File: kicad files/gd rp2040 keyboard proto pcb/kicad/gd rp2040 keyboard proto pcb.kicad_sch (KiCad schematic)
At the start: 49 parts, among them J1 USB Pwr, J10 CTRL1-HDR, J11 CTRL2-HDR, J12 USB_A, J14 GPIO, J2 Power Sequence, J3 Power, J4 FTDI Header, J5 CTRL1, J6 CTRL2, J7 Addr_Main_Data, J9 Addr_Main_Data-HDR, SW1 2040 RESET, SW2 MEGA POWER, U1 MIC5504-3.3YM5, U2 W25Q128JVS, U3 RP2040, U4 74HC245, U6 74LVC2G08DP-Q100H, U7 74LVC2G08DP-Q100H, U8 74LVC2G08DP-Q100H, Y1 ECS-120-18-33-JEM-TR

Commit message: almost done...
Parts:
- removed U6, U7, U8: 74LVC2G08DP-Q100H, Package_SO:TSSOP-8_3x3mm_P0.65mm, symbol 74xGxx:74LVC2G08
- added D5: 5V_PWR, LED_SMD:LED_1206_3216Metric, symbol My Library:D_1206
- added D8: 3V3_PWR, LED_SMD:LED_1206_3216Metric, symbol My Library:D_1206
- added Q9: BC817, Package_TO_SOT_SMD:SOT-23, symbol Transistor_BJT:BC817
- added R20, R23: 1K, Resistor_SMD:R_0805_2012Metric, symbol My_Library:R_0805
- added R28, R29: 4k7, Resistor_SMD:R_0805_2012Metric, symbol My_Library:R_0805
- added TP1, TP2, TP3: TestPoint_Harwin, My Libraries:Harwin-S1751-46-Test-Point, symbol My Library:TestPoint_Harwin
- added U10, U11, U14: 74LVC2G04, Package_TO_SOT_SMD:SOT-363_SC-70-6, symbol 74xGxx:74LVC2G04
- added U12, U13: 74LVC2G32, Package_SO:VSSOP-8_2.4x2.1mm_P0.5mm, symbol 74xGxx:74LVC2G32
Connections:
- net +3V3: now also R23.1, TP2.1, U10.5 (+3V3), U10.5 (+3V3), U11.5 (+3V3), U11.5 (+3V3), U12.8 (+3V3), U12.8 (+3V3), U13.8 (+3V3), U13.8 (+3V3), U14.5 (+3V3), U14.5 (+3V3)
- net +5V: now also R20.1, R29.2, TP1.1
- net 245_EN: now also TP3.1
- net GND: now also D5.1 (K), D8.1 (K), Q9.2 (E), U10.2 (GND), U10.2 (GND), U11.2 (GND), U11.2 (GND), U12.4 (GND), U12.4 (GND), U13.4 (GND), U13.4 (GND), U13.5, U13.6, U14.2 (GND), U14.2 (GND)
- net KSEL0: now also U13.2
- net KSEL0rp: now also U13.7
- net KSEL1: now also U12.6
- net KSEL1rp: now also U12.3
- net KSEL2: now also U12.2
- net KSEL2rp: now also U12.7
- net PH0: now also U14.1
- net PH0rp: now also U14.4
- net RESETrp: now also U11.6
- net RW: now also U10.3
- net RWrp: now also U10.6
- net ~{RESET}: now also Q9.3 (C), R29.1, U11.3
- net GPIO18: no longer names the net of J14.6 (Pin_6)
- net GPIO18: no longer U3.29 (GPIO18)
- net TXen: no longer names the net of U3.37 (GPIO25)
- new net: Q9.1 (B), R28.1
- new net: D5.2 (A), R20.2
- new net: D8.2 (A), R23.2
- new net: U11.1, U11.4
- new net: U10.1, U10.4
- new net RESET_CTL: R28.2, U3.29 (GPIO18)
- new net ~{PH0}: U12.1, U12.5, U13.1, U14.3, U14.6
- no-connect marks 0 -> 1
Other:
- moved on the sheet: C2, C3, Ctx1, Ctx2, J14, R5, Y1

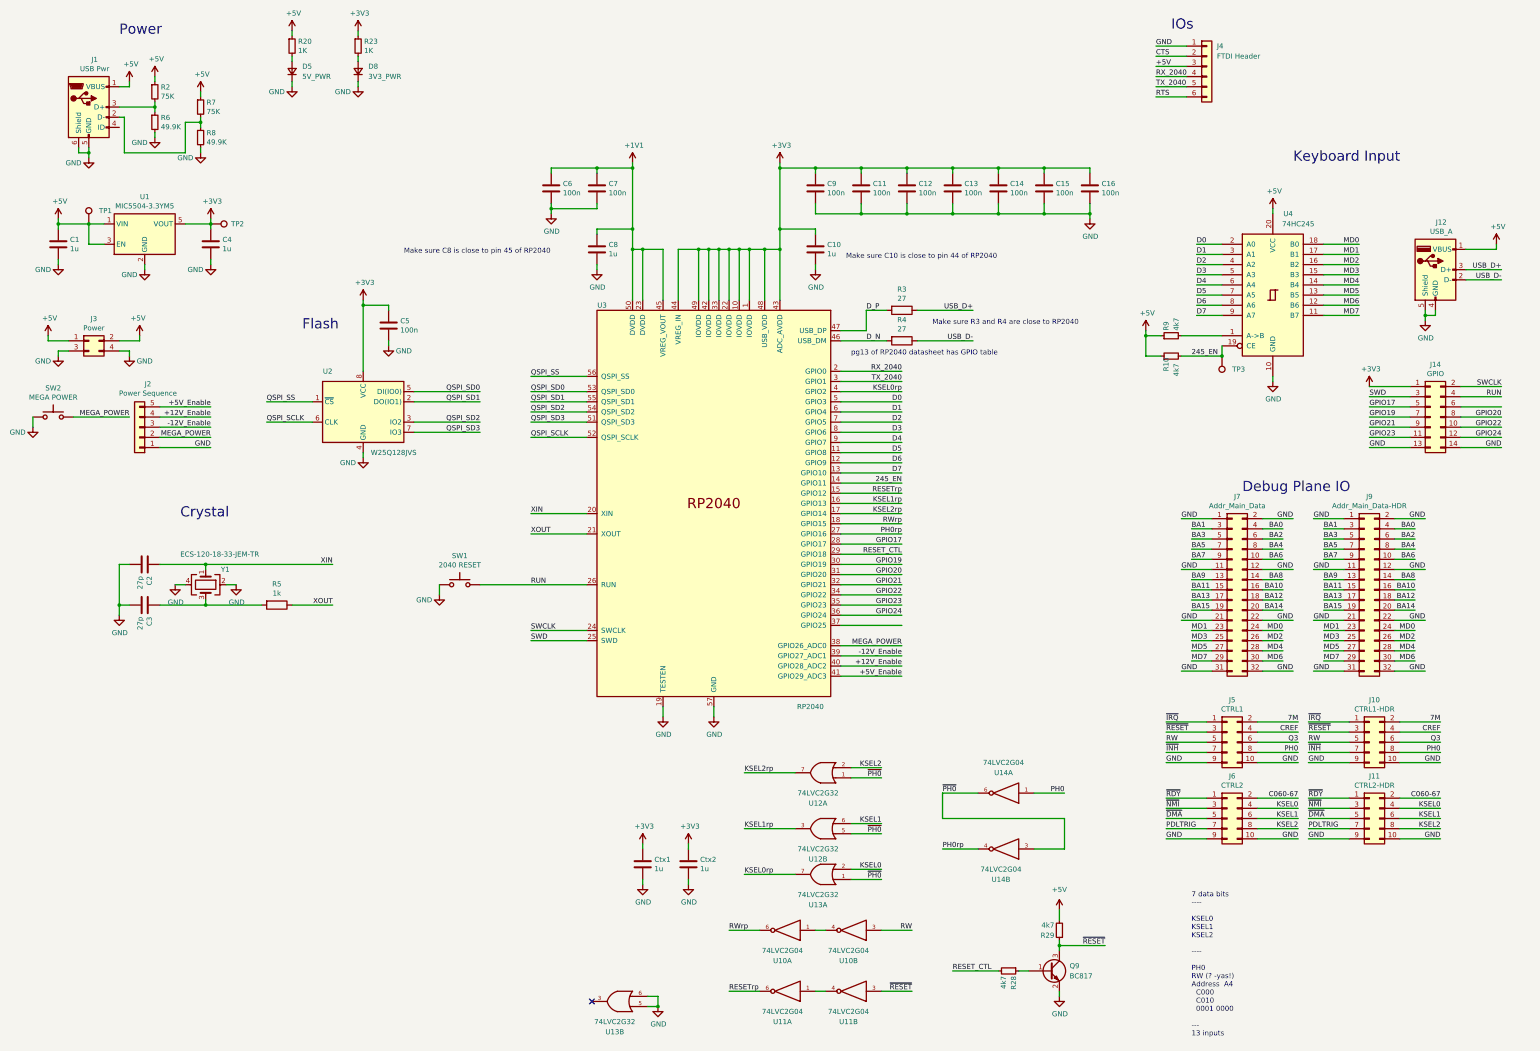
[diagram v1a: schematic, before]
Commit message: rev3 with 573 buffer for gating KSEL and RW
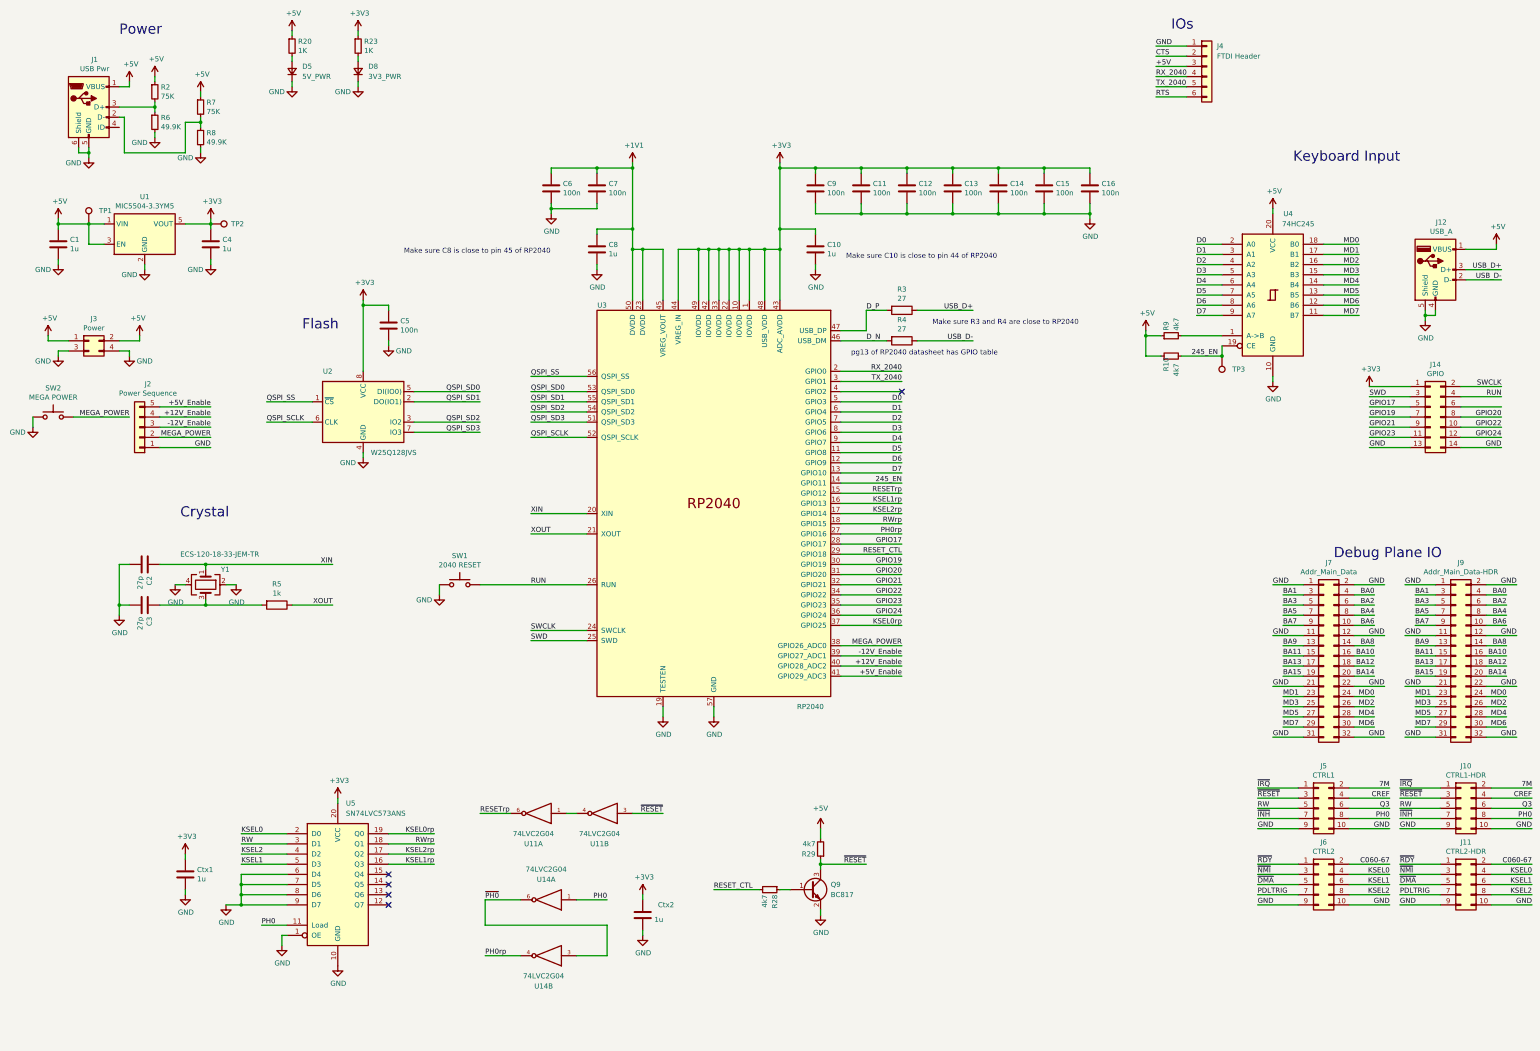
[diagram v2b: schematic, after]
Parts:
- removed U10: 74LVC2G04, Package_TO_SOT_SMD:SOT-363_SC-70-6, symbol 74xGxx:74LVC2G04
- removed U12, U13: 74LVC2G32, Package_SO:VSSOP-8_2.4x2.1mm_P0.5mm, symbol 74xGxx:74LVC2G32
- added U5: SN74LVC573ANS, Package_SO:SO-20_5.3x12.6mm_P1.27mm, symbol 74xx:74LS573
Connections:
- net +3V3: now also U5.20 (VCC)
- net GND: now also U5.1 (OE), U5.10 (GND), U5.6 (D4), U5.7 (D5), U5.8 (D6), U5.9 (D7)
- net KSEL0: now also U5.2 (D0)
- net KSEL0rp: now also U3.37 (GPIO25), U5.19 (Q0); no longer U3.4 (GPIO2)
- net KSEL1: now also U5.5 (D3)
- net KSEL1rp: now also U5.16 (Q3)
- net KSEL2: now also U5.4 (D2)
- net KSEL2rp: now also U5.17 (Q2)
- net PH0: now also U5.11 (Load)
- net RW: now also U5.3 (D1)
- net RWrp: now also U5.18 (Q1)
- no-connect marks 1 -> 5
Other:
- note removed: "7 data bits ---- KSEL0 KSEL1 KSEL2 ---- PH0 RW (? -yas!) Address A4 C000 C010 0001 0000 --- 13 inputs"
- company: (none) -> twitch.tv/baldengineer
- title: RP2040 for Mini IIe Proto -> RP2040 for Mega IIe Proto Rev2
- moved on the sheet: Ctx1, Ctx2, J10, J11, J5, J6, J7, J9, Q9, R28, R29, U11A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

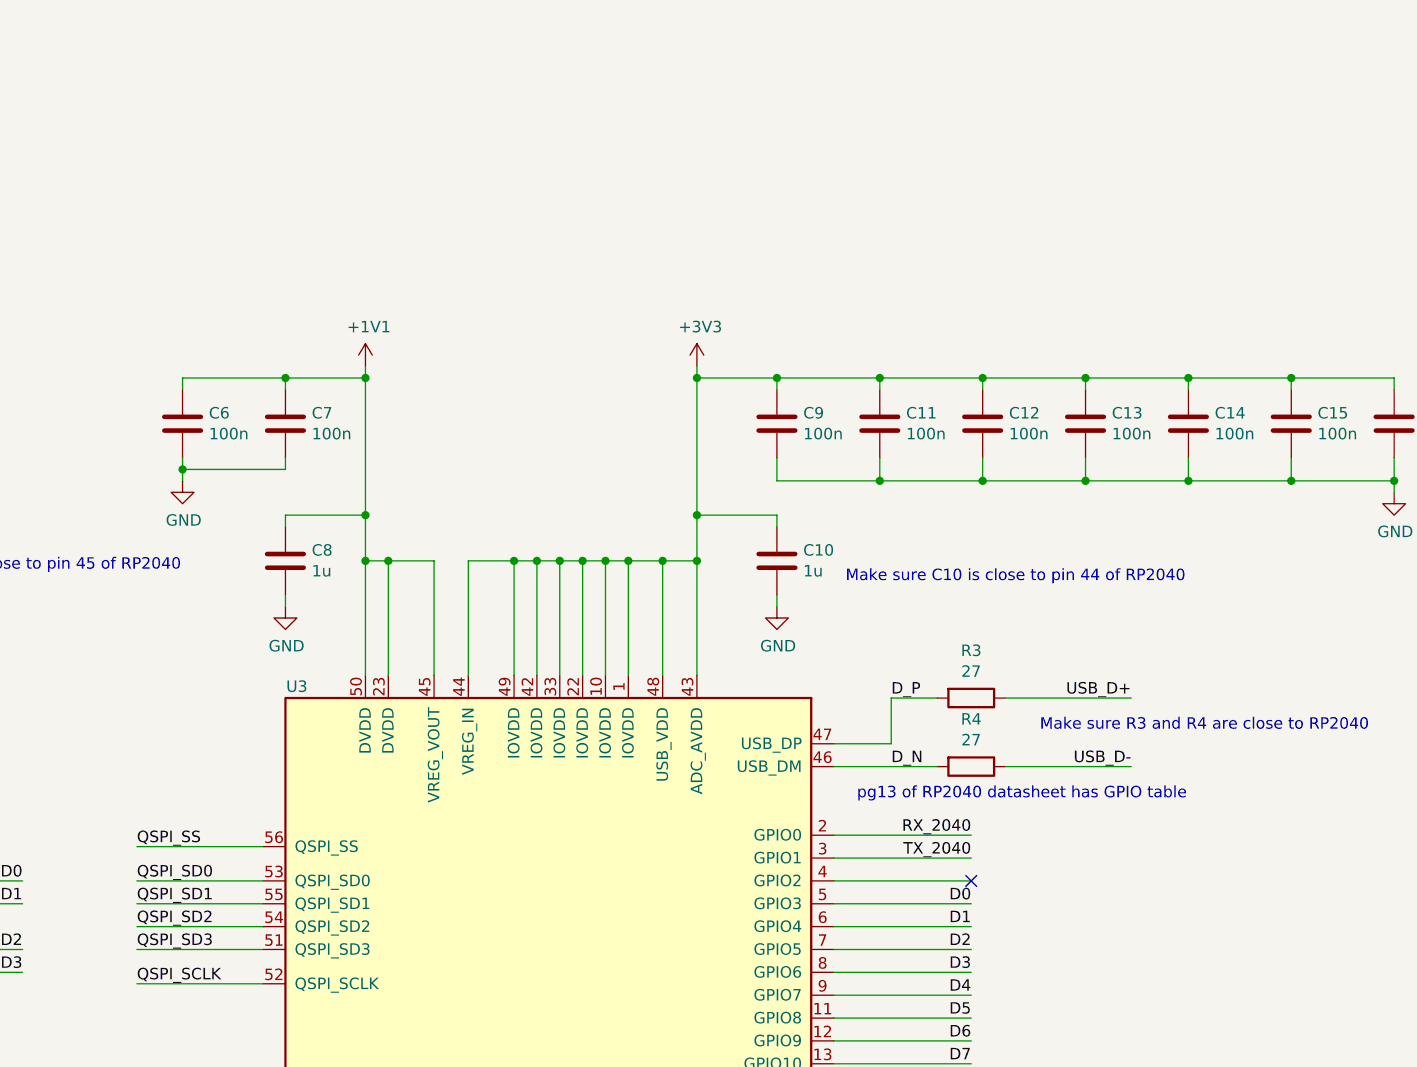
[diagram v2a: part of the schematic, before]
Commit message: added test point for GPIO2 (former KSEL0) -- Tim said I could!
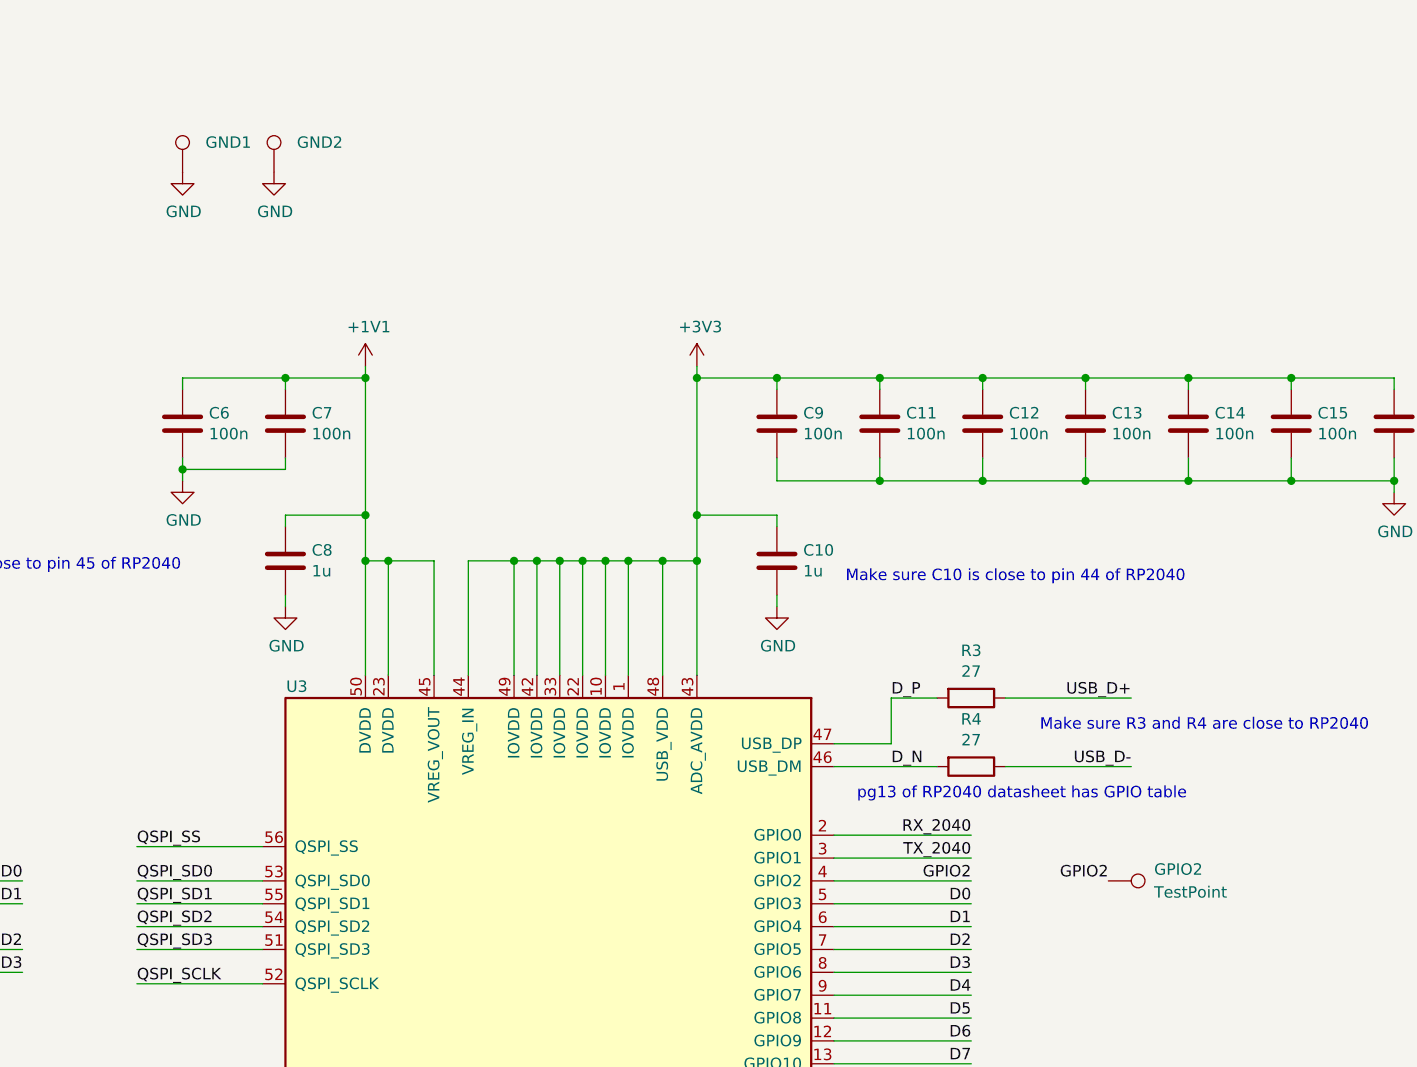
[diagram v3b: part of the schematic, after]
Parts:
- added GND1, GND2: TestPoint_Harwin, My Libraries:Harwin-S1751-46-Test-Point, symbol My Library:TestPoint_Harwin
- added GPIO2: TestPoint, TestPoint:TestPoint_Pad_D1.0mm, symbol Connector:TestPoint
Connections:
- net GND: now also GND1.1, GND2.1
- net GPIO2: now reaches U3.4 (GPIO2)
- net GPIO2: now also GPIO2.1
- no-connect marks 5 -> 4
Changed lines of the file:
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@@
   (junction (at 199.39 81.28) (diameter 0) (color 0 0 0 0)
   )
-  (no_connect (at 245.11 116.84))
   (no_connect (at 116.84 240.03))
   (no_connect (at 116.84 237.49))
@@
     (stroke (width 0) (type default) (color 0 0 0 0))
   )
-  (wire (pts (xy 229.87 116.84) (xy 245.11 116.84))
-    (stroke (width 0) (type default) (color 0 0 0 0))
-  )
   (wire (pts (xy 80.01 229.87) (xy 91.44 229.87))
     (stroke (width 0) (type default) (color 0 0 0 0))
@@
     (stroke (width 0) (type default) (color 0 0 0 0))
   )
+  (wire (pts (xy 229.87 116.84) (xy 245.11 116.84))
+    (stroke (width 0) (type default) (color 0 0 0 0))
+  )
   (wire (pts (xy 391.16 198.12) (xy 396.24 198.12))
     (stroke (width 0) (type default) (color 0 0 0 0))
@@
     (effects (font (size 1.27 1.27)) (justify left bottom))
   )
+  (label "GPIO2" (at 260.35 116.84 180)
+    (effects (font (size 1.27 1.27)) (justify right bottom))
+  )
   (label "BA6" (at 363.22 175.26 180)
     (effects (font (size 1.27 1.27)) (justify right bottom))
@@
     (effects (font (size 1.27 1.27)) (justify left bottom))
   )
+  (label "GPIO2" (at 245.11 116.84 180)
+    (effects (font (size 1.27 1.27)) (justify right bottom))
+  )
   (label "GPIO22" (at 394.97 125.73 180)
     (effects (font (size 1.27 1.27)) (justify right bottom))
@@
     (pin "2")
   )
+  (symbol (lib_id "My Library:TestPoint_Harwin") (at 167.64 38.1 0) (unit 1)
+    (in_bom yes) (on_board yes) (fields_autoplaced)
+    (property "Reference" "GND2" (id 0) (at 170.18 34.7979 0)
+      (effects (font (size 1.27 1.27)) (justify left))
+    )
+    (property "Value" "TestPoint_Harwin" (id 1) (at 167.64 33.02 0)
+      (effects (font (size 1.27 1.27)) hide)
+    )
+    (property "Footprint" "My Libraries:Harwin-S1751-46-Test-Point" (id 2) (at 172.72 38.1 0)
+      (effects (font (size 1.27 1.27)) hide)
+    )
+    (property "Datasheet" "~" (id 3) (at 172.72 38.1 0)
+      (effects (font (size 1.27 1.27)) hide)
+    )
+    (pin "1")
+  )
   (symbol (lib_id "My_Library:R_0805") (at 224.79 231.14 180) (unit 1)
     (in_bom yes) (on_board yes)
@@
     (pin "2")
   )
+  (symbol (lib_id "power:GND") (at 157.48 38.1 0) (unit 1)
+    (in_bom yes) (on_board yes)
+    (property "Reference" "#PWR?" (id 0) (at 157.48 44.45 0)
+      (effects (font (size 1.27 1.27)) hide)
+    )
+    (property "Value" "GND" (id 1) (at 157.607 42.4942 0))
+    (property "Footprint" "" (id 2) (at 157.48 38.1 0)
+      (effects (font (size 1.27 1.27)) hide)
+    )
+    (property "Datasheet" "" (id 3) (at 157.48 38.1 0)
+      (effects (font (size 1.27 1.27)) hide)
+    )
+    (pin "1")
+  )
   (symbol (lib_id "power:+3V3") (at 104.14 218.44 0) (unit 1)
     (in_bom yes) (on_board yes)
@@
     (pin "1")
   )
+  (symbol (lib_id "My Library:TestPoint_Harwin") (at 157.48 38.1 0) (unit 1)
+    (in_bom yes) (on_board yes) (fields_autoplaced)
+    (property "Reference" "GND1" (id 0) (at 160.02 34.7979 0)
+      (effects (font (size 1.27 1.27)) (justify left))
+    )
+    (property "Value" "TestPoint_Harwin" (id 1) (at 157.48 33.02 0)
+      (effects (font (size 1.27 1.27)) hide)
+    )
+    (property "Footprint" "My Libraries:Harwin-S1751-46-Test-Point" (id 2) (at 162.56 38.1 0)
+      (effects (font (size 1.27 1.27)) hide)
+    )
+    (property "Datasheet" "~" (id 3) (at 162.56 38.1 0)
+      (effects (font (size 1.27 1.27)) hide)
+    )
+    (pin "1")
+  )
   (symbol (lib_name "74LVC2G04_1") (lib_id "74xGxx:74LVC2G04") (at 156.21 257.81 180) (unit 2)
     (in_bom yes) (on_board yes) (fields_autoplaced)
@@
     (pin "4")
   )
+  (symbol (lib_id "Connector:TestPoint") (at 260.35 116.84 270) (unit 1)
+    (in_bom yes) (on_board yes) (fields_autoplaced)
+    (property "Reference" "GPIO2" (id 0) (at 265.43 115.5699 90)
+      (effects (font (size 1.27 1.27)) (justify left))
+    )
+    (property "Value" "TestPoint" (id 1) (at 265.43 118.1099 90)
+      (effects (font (size 1.27 1.27)) (justify left))
+    )
+    (property "Footprint" "TestPoint:TestPoint_Pad_D1.0mm" (id 2) (at 260.35 121.92 0)
+      (effects (font (size 1.27 1.27)) hide)
+    )
+    (property "Datasheet" "~" (id 3) (at 260.35 121.92 0)
+      (effects (font (size 1.27 1.27)) hide)
+    )
+    (pin "1")
+  )
   (symbol (lib_id "power:GND") (at 90.17 255.27 0) (unit 1)
     (in_bom yes) (on_board yes)
@@
     (pin "1")
   )
+  (symbol (lib_id "power:GND") (at 167.64 38.1 0) (unit 1)
+    (in_bom yes) (on_board yes)
+    (property "Reference" "#PWR?" (id 0) (at 167.64 44.45 0)
+      (effects (font (size 1.27 1.27)) hide)
+    )
+    (property "Value" "GND" (id 1) (at 167.767 42.4942 0))
+    (property "Footprint" "" (id 2) (at 167.64 38.1 0)
+      (effects (font (size 1.27 1.27)) hide)
+    )
+    (property "Datasheet" "" (id 3) (at 167.64 38.1 0)
+      (effects (font (size 1.27 1.27)) hide)
+    )
+    (pin "1")
+  )
   (symbol (lib_id "power:GND") (at 224.79 247.65 0) (unit 1)
     (in_bom yes) (on_board yes)
@@
       (reference "#PWR0118") (unit 1) (value "+3V3") (footprint "")
     )
+    (path "/8c777cdc-3cd1-41aa-8be9-b9db0da4cd2a"
+      (reference "#PWR?") (unit 1) (value "GND") (footprint "")
+    )
+    (path "/c8fa22bf-9f7d-4a3d-8da3-a1f24f794fe0"
+      (reference "#PWR?") (unit 1) (value "GND") (footprint "")
+    )
     (path "/00000000-0000-0000-0000-00005f09255d"
       (reference "C1") (unit 1) (value "1u") (footprint "Capacitor_SMD:C_0805_2012Metric")
@@
       (reference "D8") (unit 1) (value "3V3_PWR") (footprint "LED_SMD:LED_1206_3216Metric")
     )
+    (path "/99603f10-b974-41e5-92ba-917200586878"
+      (reference "GND1") (unit 1) (value "TestPoint_Harwin") (footprint "My Libraries:Harwin-S1751-46-Test-Point")
+    )
+    (path "/6d1fad75-390f-42e2-9cf8-0986f5882f7b"
+      (reference "GND2") (unit 1) (value "TestPoint_Harwin") (footprint "My Libraries:Harwin-S1751-46-Test-Point")
+    )
+    (path "/a6e63ee2-6cde-4eb1-8264-4356edd05627"
+      (reference "GPIO2") (unit 1) (value "TestPoint") (footprint "TestPoint:TestPoint_Pad_D1.0mm")
+    )
     (path "/00000000-0000-0000-0000-0000614d9fdf"
